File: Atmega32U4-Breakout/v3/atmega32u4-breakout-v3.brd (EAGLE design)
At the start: 39.1 x 21.3 mm, 54 parts, among them U1 ATMEGA32U4

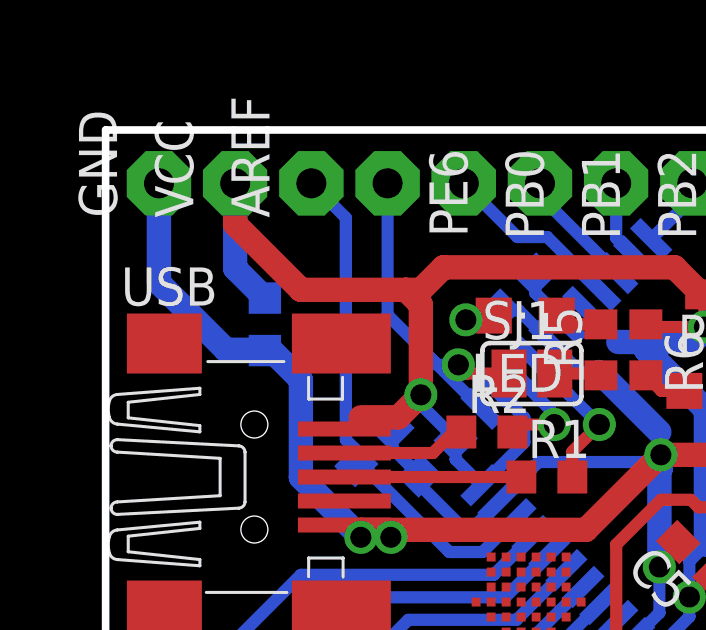
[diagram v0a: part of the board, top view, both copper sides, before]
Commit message: - Add silkscreen line between LED resistors so their orientation becomes   more clear. - Change green LED resistor to 150R - Change input filter cap to 0805 4.7uF - Match BOM
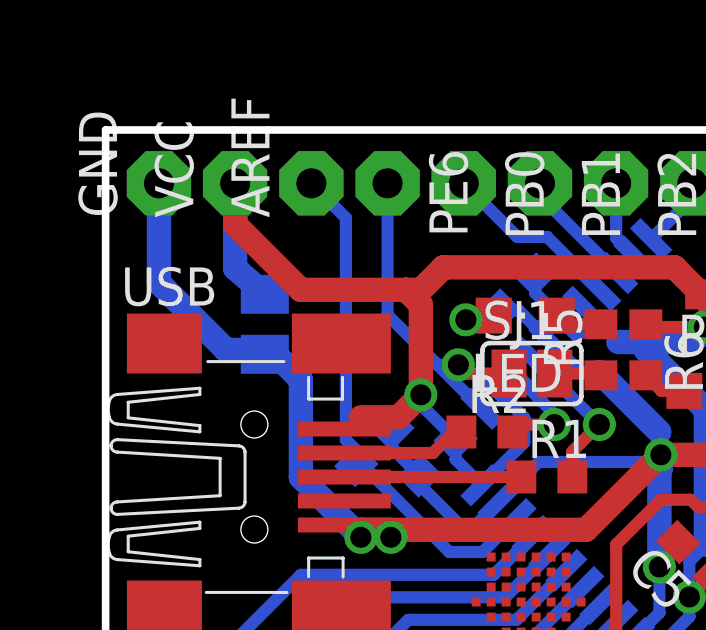
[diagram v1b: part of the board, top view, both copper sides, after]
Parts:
- C9: value 1u -> 4.7u; device rcl:C0603K -> rcl:C0805K
- LED: value (none) -> RED
- POWER: value (none) -> GREEN
- R6: value 180 -> 150
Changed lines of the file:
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@@
 <?xml version="1.0" encoding="utf-8"?>
 <!DOCTYPE eagle SYSTEM "eagle.dtd">
-<eagle version="6.0">
+<eagle version="6.1">
 <drawing>
 <settings>
@@
 <grid distance="0.5" unitdist="mm" unit="mm" style="lines" multiple="1" display="no" altdistance="0.25" altunitdist="mm" altunit="mm"/>
 <layers>
-<layer number="1" name="Top" color="4" fill="1" visible="yes" active="yes"/>
+<layer number="1" name="Top" color="4" fill="1" visible="no" active="yes"/>
 <layer number="16" name="Bottom" color="1" fill="1" visible="yes" active="yes"/>
 <layer number="17" name="Pads" color="2" fill="1" visible="yes" active="yes"/>
@@
 <layer number="19" name="Unrouted" color="6" fill="1" visible="yes" active="yes"/>
 <layer number="20" name="Dimension" color="15" fill="1" visible="yes" active="yes"/>
-<layer number="21" name="tPlace" color="7" fill="1" visible="yes" active="yes"/>
+<layer number="21" name="tPlace" color="7" fill="1" visible="no" active="yes"/>
 <layer number="22" name="bPlace" color="7" fill="1" visible="yes" active="yes"/>
-<layer number="23" name="tOrigins" color="15" fill="1" visible="yes" active="yes"/>
+<layer number="23" name="tOrigins" color="15" fill="1" visible="no" active="yes"/>
 <layer number="24" name="bOrigins" color="15" fill="1" visible="yes" active="yes"/>
 <layer number="25" name="tNames" color="7" fill="1" visible="no" active="yes"/>
@@
 <layer number="38" name="bTest" color="7" fill="1" visible="no" active="yes"/>
 <layer number="39" name="tKeepout" color="4" fill="11" visible="no" active="yes"/>
-<layer number="40" name="bKeepout" color="1" fill="11" visible="no" active="yes"/>
-<layer number="41" name="tRestrict" color="4" fill="10" visible="yes" active="yes"/>
+<layer number="40" name="bKeepout" color="1" fill="11" visible="yes" active="yes"/>
+<layer number="41" name="tRestrict" color="4" fill="10" visible="no" active="yes"/>
 <layer number="42" name="bRestrict" color="1" fill="10" visible="yes" active="yes"/>
 <layer number="43" name="vRestrict" color="2" fill="10" visible="yes" active="yes"/>
@@
 <layer number="49" name="Reference" color="7" fill="1" visible="yes" active="yes"/>
 <layer number="50" name="dxf" color="7" fill="1" visible="yes" active="yes"/>
-<layer number="51" name="tDocu" color="7" fill="1" visible="yes" active="yes"/>
+<layer number="51" name="tDocu" color="7" fill="1" visible="no" active="yes"/>
 <layer number="52" name="bDocu" color="7" fill="1" visible="yes" active="yes"/>
 <layer number="53" name="tGND_GNDA" color="7" fill="9" visible="no" active="no"/>
@@
 <layer number="101" name="Patch_Top" color="12" fill="4" visible="yes" active="yes"/>
 <layer number="102" name="Vscore" color="7" fill="1" visible="yes" active="yes"/>
-<layer number="103" name="fp3" color="7" fill="1" visible="yes" active="yes"/>
+<layer number="103" name="fp3" color="7" fill="1" visible="no" active="yes"/>
 <layer number="104" name="Name" color="7" fill="1" visible="yes" active="yes"/>
-<layer number="105" name="Beschreib" color="9" fill="1" visible="yes" active="yes"/>
+<layer number="105" name="Beschreib" color="9" fill="1" visible="no" active="yes"/>
 <layer number="106" name="BGA-Top" color="4" fill="1" visible="yes" active="yes"/>
 <layer number="107" name="BD-Top" color="5" fill="1" visible="yes" active="yes"/>
@@
 <text x="15" y="7.25" size="1.27" layer="49" font="vector" rot="SR180">shack</text>
 <rectangle x1="9.75" y1="3.5" x2="16.5" y2="7.5" layer="41"/>
+<wire x1="17.25" y1="12.5" x2="17.25" y2="15.5" width="0.254" layer="49"/>
 </plain>
 <attributes>
@@
 <element name="C7" library="rcl" package="C0603" value="100n" x="11.068" y="10.418" rot="MR315"/>
 <element name="C8" library="rcl" package="C0603" value="100n" x="27.858" y="9.798" rot="MR45"/>
-<element name="C9" library="rcl" package="C0603K" value="1u" x="5.308" y="14.858" rot="MR270"/>
+<element name="C9" library="rcl" package="C0805K" value="4.7u" x="5.308" y="14.858" rot="MR270"/>
 <element name="PB0" library="jocki" package="2,15/1,0-NOPLACE" value="WIREPAD2,15/1,0-NOPLACE" x="11.938" y="19.558" rot="R270"/>
 <element name="PB1" library="jocki" package="2,15/1,0-NOPLACE" value="WIREPAD2,15/1,0-NOPLACE" x="14.478" y="19.558" rot="R270"/>
@@
 <element name="VCC" library="jocki" package="2,15/1,0-NOPLACE" value="WIREPAD2,15/1,0-NOPLACE" x="4.318" y="19.558" rot="R90"/>
 <element name="R5" library="rcl" package="R0603" value="180" x="16.508" y="14.008" rot="R90"/>
-<element name="R6" library="rcl" package="R0603" value="180" x="18.008" y="14.008" rot="R270"/>
+<element name="R6" library="rcl" package="R0603" value="150" x="18.008" y="14.008" rot="R270"/>
 <element name="SJ1" library="jumper" package="SJ" value="" x="14.208" y="13.218"/>
-<element name="LED" library="led" package="CHIPLED_0805" value="" x="13.988" y="15.148" rot="R90"/>
-<element name="POWER" library="led" package="CHIPLED_0805" value="" x="20.338" y="12.638" rot="R270"/>
+<element name="LED" library="led" package="CHIPLED_0805" value="RED" x="13.988" y="15.148" rot="R90"/>
+<element name="POWER" library="led" package="CHIPLED_0805" value="GREEN" x="20.338" y="12.638" rot="R270"/>
 <element name="BOOT" library="jocki" package="KMR2NG" value="SMDSWITCHKMR2" x="35.008" y="8.008"/>
 <element name="R4" library="rcl" package="R0603" value="10k" x="31.358" y="6.578" rot="R90"/>
@@
 <wire x1="10.008" y1="16.008" x2="10.508" y2="15.508" width="0.8128" layer="1"/>
 <wire x1="10.508" y1="15.508" x2="10.508" y2="12.508" width="0.8128" layer="1"/>
-<wire x1="5.308" y1="15.733" x2="4.318" y2="16.723" width="0.8128" layer="16"/>
+<wire x1="5.308" y1="15.858" x2="4.318" y2="16.723" width="0.8128" layer="16"/>
 <wire x1="4.318" y1="16.723" x2="4.318" y2="19.558" width="0.8128" layer="16"/>
 <wire x1="10.508" y1="12.508" x2="9.758" y2="11.758" width="0.8128" layer="1"/>
@@
 <wire x1="6.508" y1="9.758" x2="6.508" y2="13.008" width="0.8128" layer="16"/>
 <wire x1="6.508" y1="13.008" x2="5.533" y2="13.983" width="0.8128" layer="16"/>
-<wire x1="5.533" y1="13.983" x2="5.308" y2="13.983" width="0.4064" layer="16"/>
-<wire x1="5.308" y1="13.983" x2="5.283" y2="14.008" width="0.4064" layer="16"/>
+<wire x1="5.533" y1="13.983" x2="5.308" y2="13.858" width="0.4064" layer="16"/>
+<wire x1="5.308" y1="13.858" x2="5.283" y2="14.008" width="0.4064" layer="16"/>
 <wire x1="5.283" y1="14.008" x2="4.008" y2="14.008" width="0.8128" layer="16"/>
 <wire x1="4.008" y1="14.008" x2="1.778" y2="16.238" width="0.8128" layer="16"/>

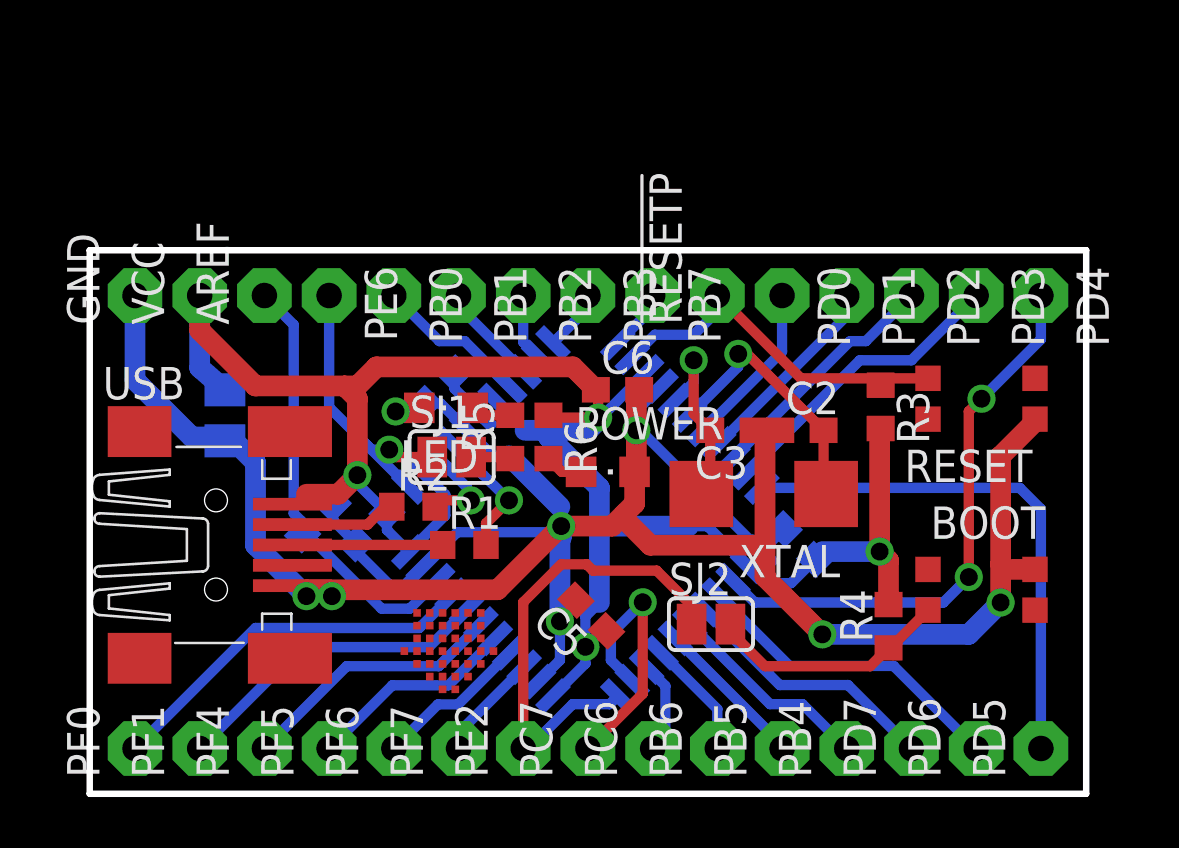
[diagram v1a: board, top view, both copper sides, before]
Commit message: Straighten a few bits of the layout, adapt to switches with ground pin. Also, match BOM.
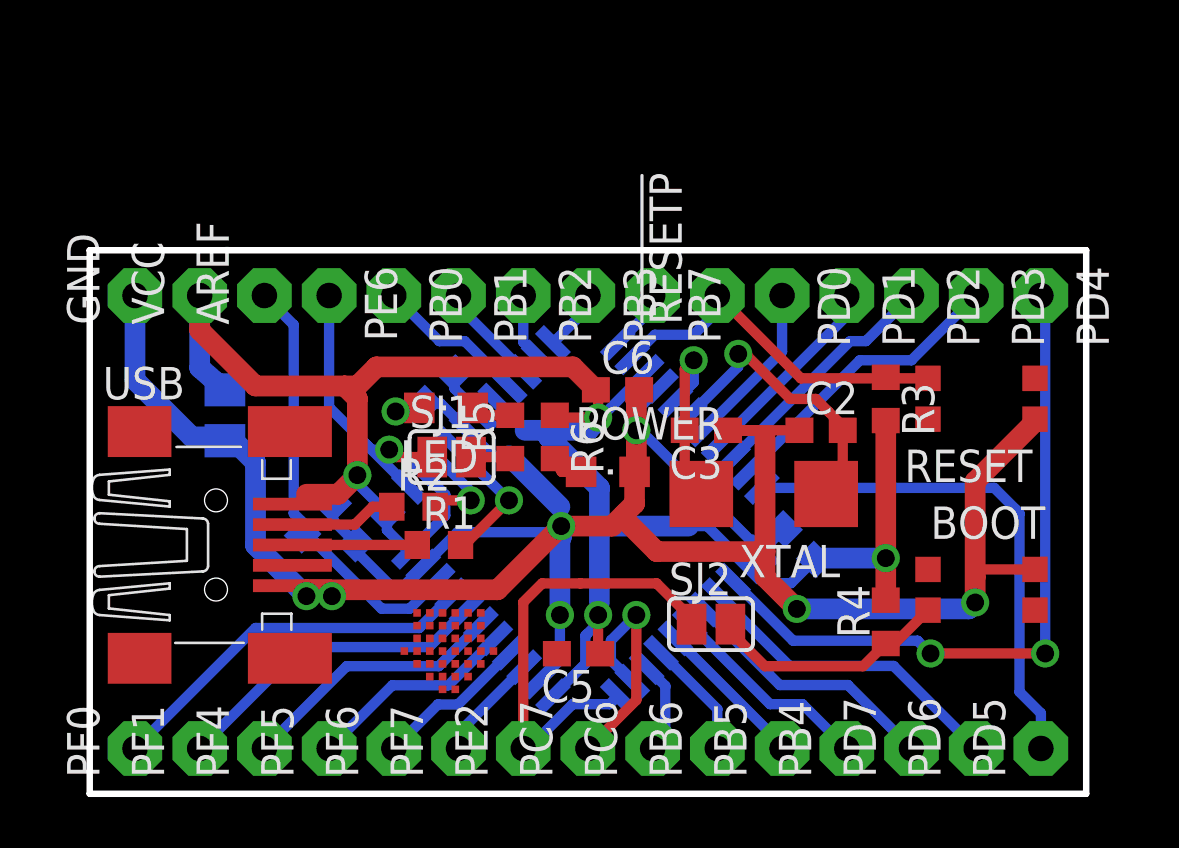
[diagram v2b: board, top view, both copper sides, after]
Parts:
- BOOT, RESET: value SMDSWITCHKMR2 -> SMDSWITCHKMR2NG
- moved C5 1.58 mm to (19.2, 5.50), turned to 180 degrees
- moved C3 1.00 mm to (24.2, 14.3)
- moved R1 1.00 mm to (13.7, 9.77)
- moved C2 0.75 mm to (28.7, 14.3)
- moved R3 0.37 mm to (31.2, 15.5)
- moved R6 0.25 mm to (18.3, 14.0)
- moved R4 0.20 mm to (31.2, 6.75)
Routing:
- net N$31: track 22.2 -> 27.6 mm
- net N$5: track 10.4 -> 12.1 mm
- net GND: track 110.7 -> 112.3 mm
- net N$24: track 10.6 -> 9.40 mm
- net N$1: track 5.90 -> 4.90 mm
- net !HWB: track 18.9 -> 18.0 mm
- net VCC: track 80.5 -> 81.1 mm
- net N$12: track 20.7 -> 20.1 mm
- net N$9: track 5.27 -> 5.77 mm

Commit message: TinyMega v2 with optional 3V3 supply
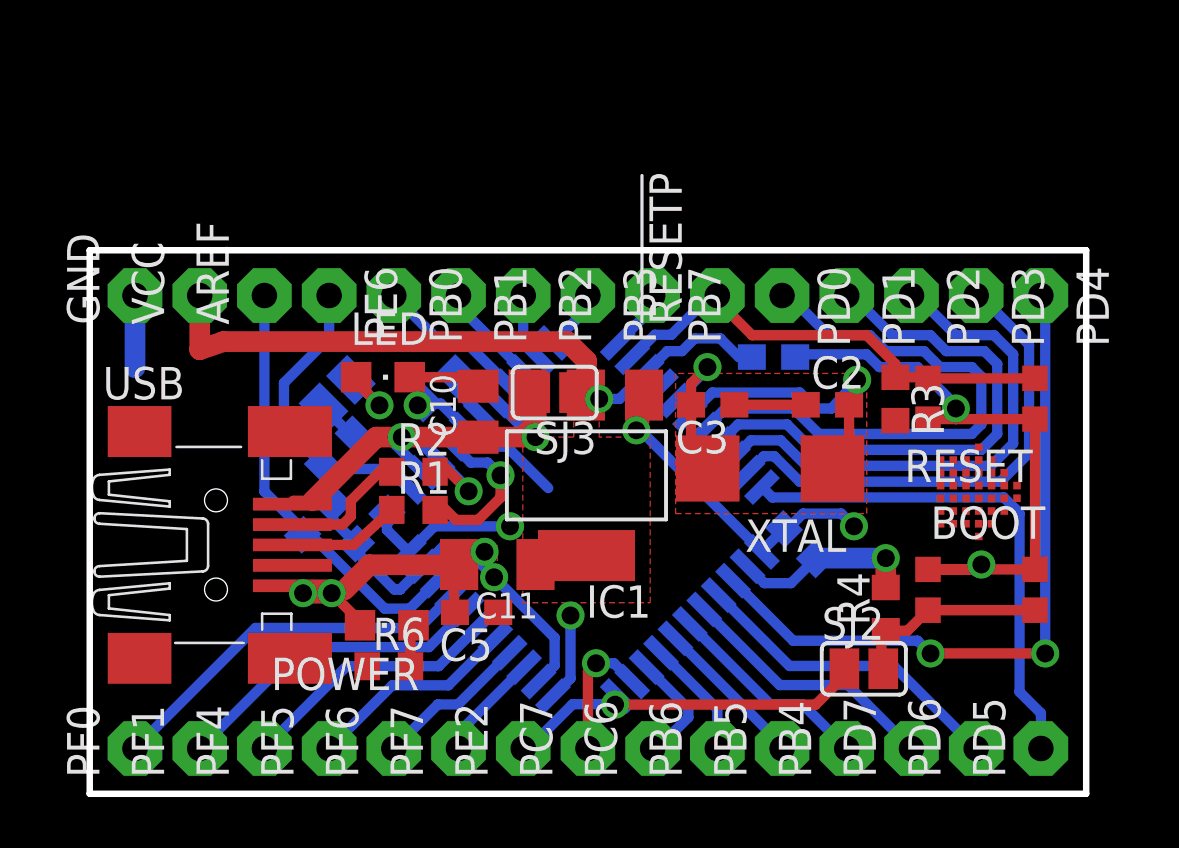
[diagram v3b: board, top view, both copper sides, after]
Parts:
- removed C9: 4.7u, rcl:C0805K
- added C10: 10u, rcl:C0805K
- added C11: 22u X7R, rcl:C1206K
- added IC1: REG1117, burr-brown:SOT223
- added SJ3: (no value), jumper:SJ
- moved R6 11.1 mm to (11.7, 5.01), turned to 0 degrees
- moved POWER 10.6 mm to (11.7, 6.61), turned to 90 degrees
- moved R5 6.78 mm to (9.75, 13.5), flipped to the bottom, turned to 135 degrees
- moved C6 6.26 mm to (26.8, 17.1), flipped to the bottom, turned to 180 degrees
- moved SJ2 6.25 mm to (30.4, 4.91)
- moved SJ1 5.13 mm to (9.72, 15.7), flipped to the bottom, turned to 135 degrees
- moved C5 4.32 mm to (15.2, 7.12)
- moved LED 2.75 mm to (11.5, 16.4), turned to 270 degrees
- moved R1 1.70 mm to (12.7, 11.1)
- moved R2 1.38 mm to (12.7, 12.6)
- moved C2 1.03 mm to (29.0, 15.3)
- moved C3 1.03 mm to (24.5, 15.3)
- moved XTAL 1.03 mm to (26.7, 12.8)
- moved R4 0.50 mm to (31.2, 7.25)
- moved R3 0.38 mm to (31.6, 15.5)
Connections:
- new net VUSB: C10.1, IC1.3, SJ3.2, U1.2, U1.7, USB.1
- net GND: now also C10.2, C11.2, IC1.1; no longer C9.2
- net LED: now also R5.1; no longer SJ1.1
- net N$11: now also SJ1.2; no longer R5.2
- net N$4: now also R5.2, SJ1.1; no longer R5.1, SJ1.2
- net VCC: now also C11.1, IC1.2, IC1.4, SJ3.1; no longer C9.1, U1.2, U1.7, USB.1
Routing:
- net VCC: track 81.1 -> 43.9 mm
- net GND: track 112.3 -> 81.2 mm, vias 8 -> 9
- net VUSB: track 0.00 -> 17.6 mm, vias 0 -> 2
- net N$27: track 6.52 -> 22.8 mm
- net N$28: track 7.90 -> 21.7 mm
- net N$29: track 9.65 -> 20.5 mm
- net N$30: track 11.9 -> 19.3 mm
- net N$24: track 9.40 -> 5.20 mm
- net !RESET: track 14.6 -> 18.6 mm
- net !HWB: track 18.0 -> 14.5 mm, vias 0 -> 1
- net N$11: track 1.72 -> 3.01 mm, vias 0 -> 1
- net N$21: track 9.52 -> 8.29 mm
- net N$6: track 7.64 -> 6.44 mm
- net N$2: track 4.19 -> 5.19 mm
- net N$23: track 3.70 -> 4.56 mm
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- added copper zone on layer 1, net VCC
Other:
- board text added: "C"
- board text removed: "C6"
- board text removed: "C7"
- board text removed: "shack"
